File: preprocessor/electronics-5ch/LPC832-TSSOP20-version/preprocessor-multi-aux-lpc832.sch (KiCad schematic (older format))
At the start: 15 parts, among them P1 ST-IN, P2 ST-OUT, P3 TH-IN, P4 TH-OUT, P5 AUX-IN, P6 LIGHT CONTROLLER, P7 AUX2-IN, P8 AUX3-IN, U1 MCP1703T-3302E/CB, U2 LPC832M101FDH20

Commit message: Correct MCU pin usage
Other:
- note added: "LPC832 pin usage:\nPIO0_0 (19, TDO, ISP-Rx) Steering input / Rx\nPIO0_1 (12, TDI) (TLC5940 GSCLK)\nPIO0_2 (8, TMS, SWDIO) (TLC5940 SCLK)\nPIO0_3 (7, TCK, SWCLK) (TLC5940 XLAT)\nPIO0_4 (6, TRST, ISP-Tx) Throttle input / Tx\nPIO0_5 (5, RESET) NC\nPIO0_6 (was TLC5940 BLANK)\nPIO0_7 (was TLC5940 SIN)\nPIO0_8 (14, XTALIN) AUX2 input\nPIO0_9 (13, XTALOUT) (Switched light output)\nPIO0_10 (10, Open drai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"
- note removed: "Light Controller pin usage:\nPIO0_0 (16, TDO, ISP-Rx) Steering input / Rx\nPIO0_1 (9, TDI) TLC5940 GSCLK\nPIO0_2 (6, TMS, SWDIO) TLC5940 SCLK\nPIO0_3 (5, TCK, SWCLK) TLC5940 XLAT\nPIO0_4 (4, TRST, ISP-Tx) Throttle input / Tx\nPIO0_5 (3, RESET) NC (test point)\nPIO0_6 (15) TLC5940 BLANK\nPIO0_7 (14) TLC5940 SIN\nPIO0_8 (11, XTALIN) ===> AUX2\nPIO0_9 (10, XTALOUT) Switched light output (for driving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"
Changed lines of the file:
@@
 Sheet 1 1
 Title "Pre-processor for RC Light Controller"
-Date "2021-04-11"
+Date "2021-05-09"
 Rev "3"
 Comp "LANE Boys RC"
@@
 Wire Wire Line
 	6150 3150 6150 3300
-Text Notes 2600 7000 0    50   ~ 0
-Light Controller pin usage:\nPIO0_0   (16, TDO, ISP-Rx)   Steering input / Rx\nPIO0_1   (9,  TDI)           TLC5940 GSCLK\nPIO0_2   (6,  TMS, SWDIO)    TLC5940 SCLK\nPIO0_3   (5,  TCK, SWCLK)    TLC5940 XLAT\nPIO0_4   (4,  TRST, ISP-Tx)  Throttle input / Tx\nPIO0_5   (3,  RESET)         NC (test point)\nPIO0_6   (15)                TLC5940 BLANK\nPIO0_7   (14)                TLC5940 SIN\nPIO0_8   (11, XTALIN)        ===> AUX2\nPIO0_9   (10, XTALOUT)       Switched light output (for driving a load via a MOSFET)\nPIO0_10  (8,  Open drain)    NC\nPIO0_11  (7,  Open drain)    ===> AUX3 (100K pull-down)\nPIO0_12  (2,  ISP-entry)     OUT / ISP\nPIO0_13  (1)                 CH3 input\n
+Text Notes 2950 7600 0    50   ~ 0
+LPC832 pin usage:\nPIO0_0   (19, TDO, ISP-Rx)   Steering input / Rx\nPIO0_1   (12, TDI)           (TLC5940 GSCLK)\nPIO0_2   (8,  TMS, SWDIO)    (TLC5940 SCLK)\nPIO0_3   (7,  TCK, SWCLK)    (TLC5940 XLAT)\nPIO0_4   (6,  TRST, ISP-Tx)  Throttle input / Tx\nPIO0_5   (5,  RESET)         NC\nPIO0_6                       (was TLC5940 BLANK)\nPIO0_7                       (was TLC5940 SIN)\nPIO0_8   (14, XTALIN)        AUX2 input\nPIO0_9   (13, XTALOUT)       (Switched light output)\nPIO0_10  (10, Open drain)    NC\nPIO0_11  (9,  Open drain)    AUX3 input\nPIO0_12  (4,  ISP-entry)     OUT / ISP\nPIO0_13  (3)                 AUX input\nPIO0_14  (20)                Hardware detection, must be floating (or high)\nPIO0_15  (11)                (TLC5940 BLANK)\nPIO0_17  (2)                 NC\nPIO0_23  (1)                 (TLC5940 SIN)\nGND      (13)\n3.3V     (12)\nVREFN    (17)\nVREFP    (18)\n
 Text Notes 6300 3200 0    50   ~ 0
 Pull-down required because \nPIO0_11 is open drain!

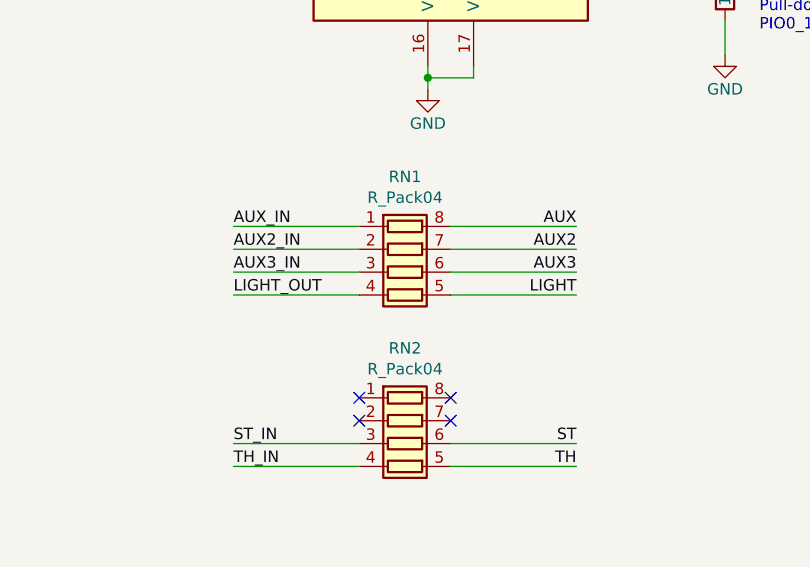
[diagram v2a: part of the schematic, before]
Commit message: Improve FAB layer and silkscreen
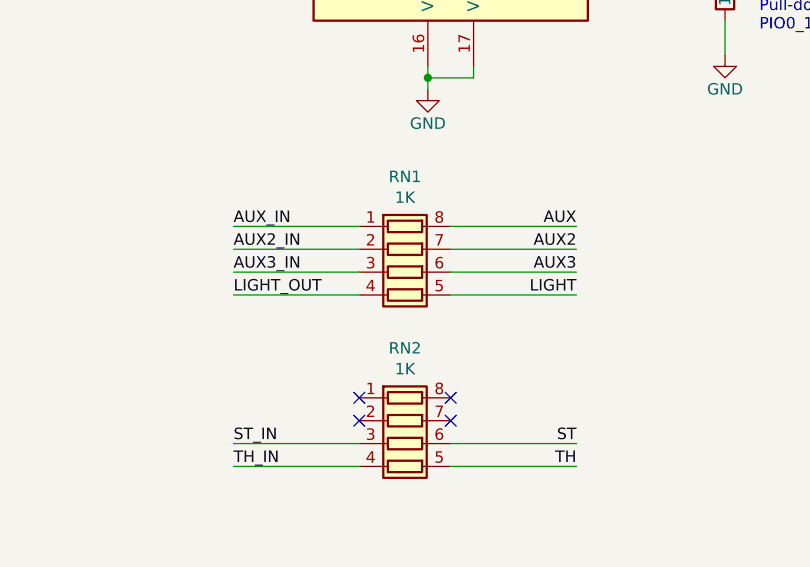
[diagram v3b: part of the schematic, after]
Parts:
- RN1, RN2: value R_Pack04 -> 1K
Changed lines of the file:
@@
 P 4750 4250
 F 0 "RN1" V 4333 4250 50  0000 C CNN
-F 1 "R_Pack04" V 4424 4250 50  0000 C CNN
+F 1 "1K" V 4424 4250 50  0000 C CNN
 F 2 "Resistor_SMD:R_Array_Convex_4x0603" V 5025 4250 50  0001 C CNN
 F 3 "~" H 4750 4250 50  0001 C CNN
@@
 P 4750 5000
 F 0 "RN2" V 4333 5000 50  0000 C CNN
-F 1 "R_Pack04" V 4424 5000 50  0000 C CNN
+F 1 "1K" V 4424 5000 50  0000 C CNN
 F 2 "Resistor_SMD:R_Array_Convex_4x0603" V 5025 5000 50  0001 C CNN
 F 3 "~" H 4750 5000 50  0001 C CNN
